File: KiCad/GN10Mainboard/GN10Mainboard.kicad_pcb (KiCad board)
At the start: 4 copper layers, 80 x 60 mm, 128 parts, among them J1 XT30PW-M, J10 USB_C_Receptacle_USB2.0, J12 Conn_01x04, J13 Conn_01x06, J14 Conn_01x06, J4 Conn_01x04, J5 Conn_01x06, J6 Conn_01x04, J7 Conn_01x04, J8 Conn_01x04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

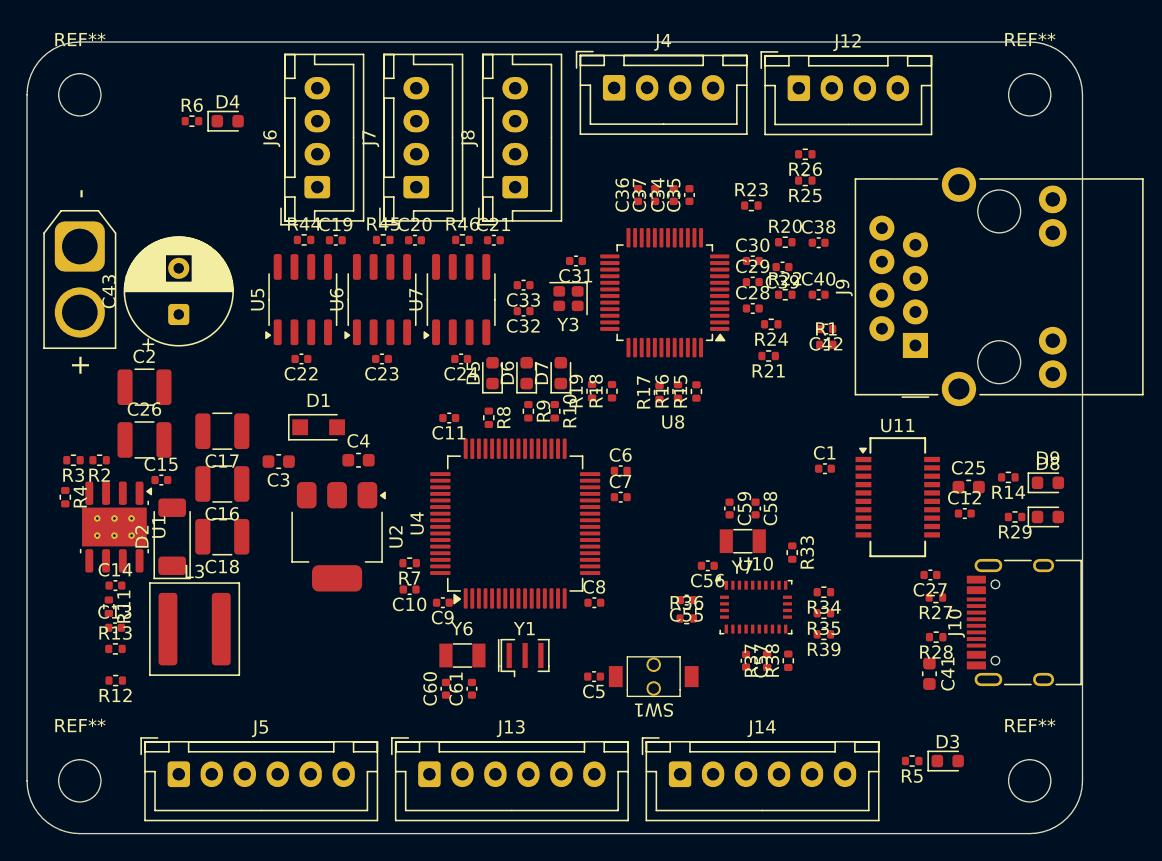
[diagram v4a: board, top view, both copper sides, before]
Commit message: update:compornents placement
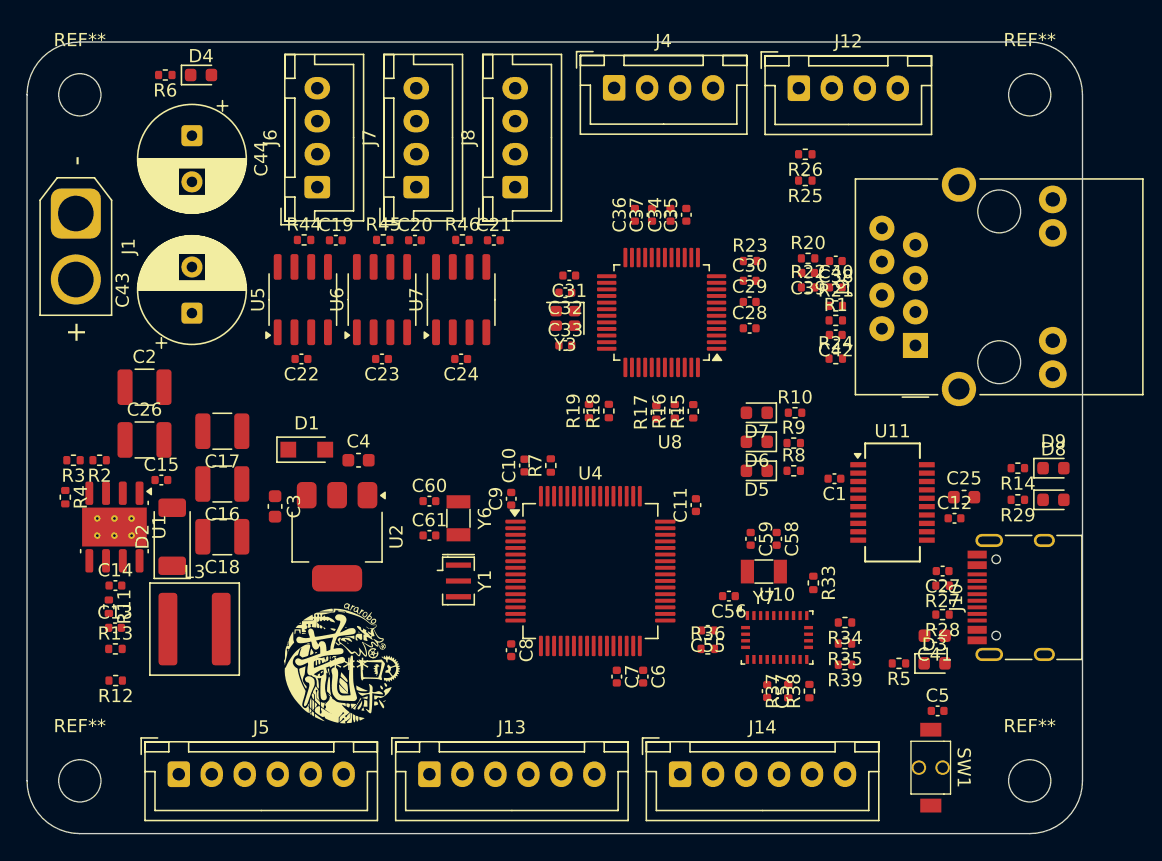
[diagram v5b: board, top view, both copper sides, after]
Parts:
- added C44: 100u, Capacitor_THT:CP_Radial_D8.0mm_P3.50mm, F.Cu at (142.5, 97.1)
- added G***: LOGO, GN10_Parts:ararobosmall, F.Cu at (153.6, 137.5)
- D2: value B560C -> RB088LAM-60TR
- moved C5 26.2 mm to (199.0, 140.7), turned to 0 degrees
- moved R8 23.5 mm to (188.1, 122.5), turned to 0 degrees
- moved SW1 22.1 mm to (198.5, 145.0), turned to -90 degrees
- moved D5 21.4 mm to (185.3, 122.5), turned to 180 degrees
- moved R9 20.3 mm to (188.1, 120.4), turned to 0 degrees
- moved C11 19.8 mm to (180.7, 125.1), turned to 90 degrees
- moved R10 18.2 mm to (188.2, 118.1), turned to 0 degrees
- moved D6 18.2 mm to (185.3, 120.3), turned to 180 degrees
- moved C6 15.7 mm to (176.7, 138.1), turned to -90 degrees
- moved D7 15.2 mm to (185.3, 118.1), turned to 180 degrees
- moved C60 14.3 mm to (160.5, 124.8), turned to 0 degrees
- moved C7 13.6 mm to (174.7, 138.1), turned to -90 degrees
- moved R7 13.0 mm to (169.7, 122.1), turned to 90 degrees
- moved C10 12.8 mm to (167.7, 122.1), turned to 90 degrees
- moved C61 12.1 mm to (160.5, 127.4), turned to 0 degrees
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
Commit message: update:components placement
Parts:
- moved R5 11.3 mm to (207.2, 139.3), turned to 0 degrees
- moved D3 6.12 mm to (204.5, 139.3), turned to 180 degrees
- moved C8 2.97 mm to (164.5, 134.1), turned to 180 degrees
- moved C17 2.81 mm to (145.0, 122.3)
- moved C16 2.11 mm to (145.0, 125.6)
- moved C43 1.66 mm to (140.8, 110.7), turned to 0 degrees
- moved C22 1.54 mm to (151.5, 115.4)
- moved C23 1.54 mm to (157.6, 115.4)
- moved C24 1.54 mm to (163.6, 115.4)
- moved C18 1.41 mm to (145.0, 128.9)
- moved U5 1.37 mm to (151.6, 110.7)
- moved U6 1.37 mm to (157.6, 110.7)
- moved U7 1.37 mm to (163.6, 110.7)
- moved C11 1.24 mm to (181.0, 126.3), turned to 0 degrees
- moved C10 1.21 mm to (168.8, 121.6)
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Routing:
- net +BATT: track 0.00 -> 8.51 mm

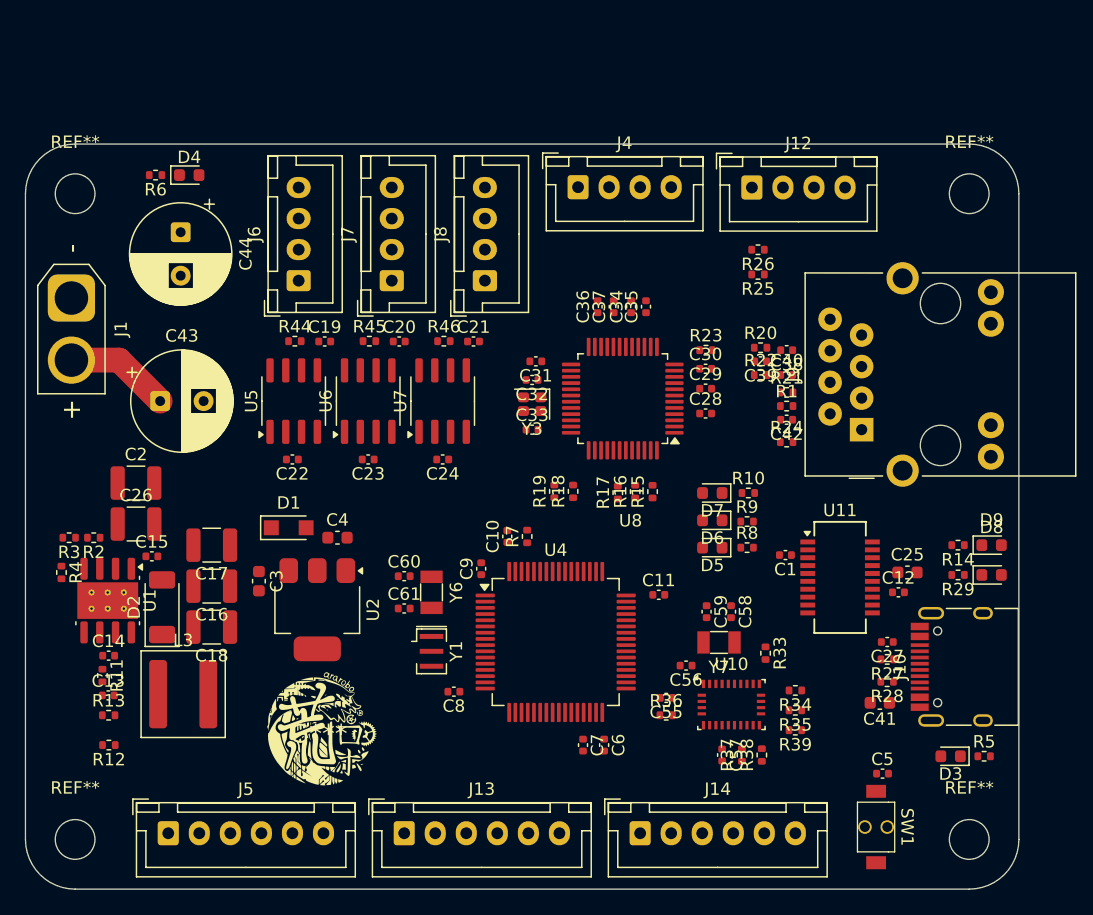
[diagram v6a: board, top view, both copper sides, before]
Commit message: add:DC/DC wiring
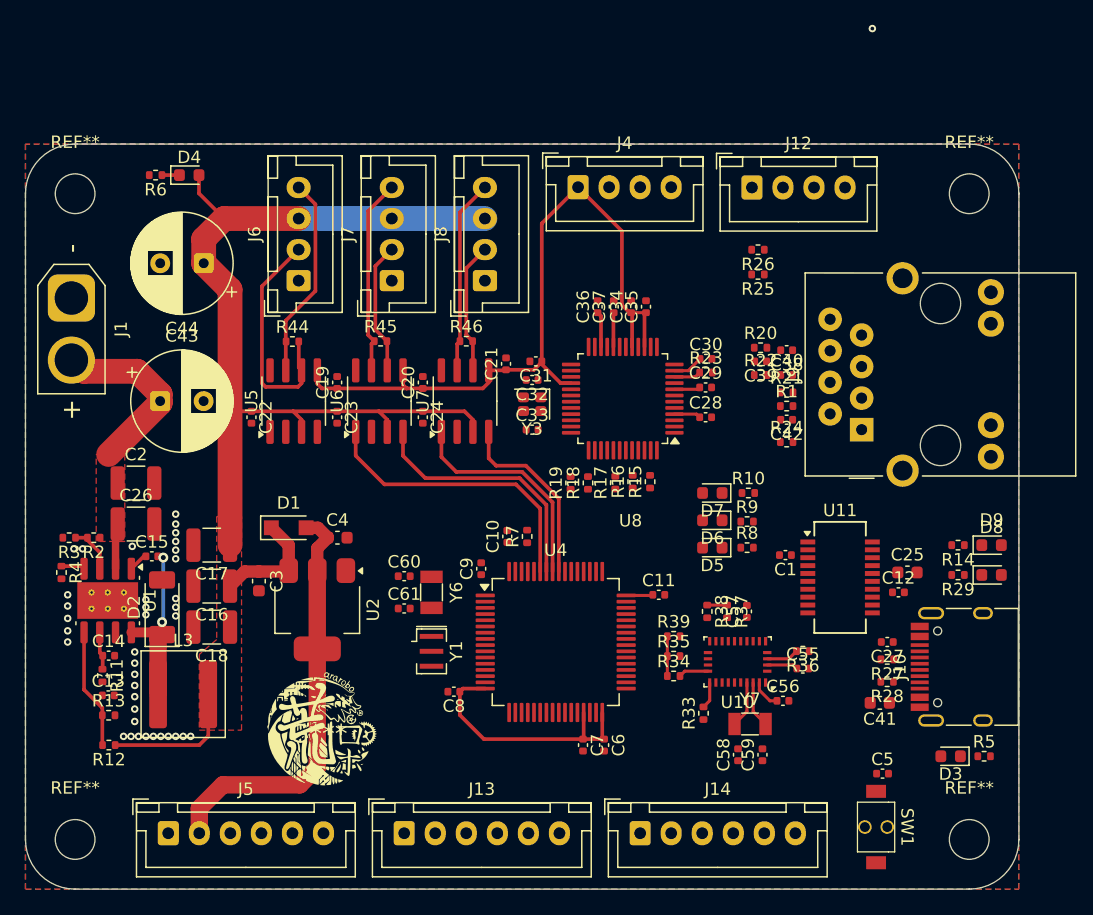
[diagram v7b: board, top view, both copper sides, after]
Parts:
- moved R39 12.4 mm to (182.2, 129.6), turned to 0 degrees
- moved R38 12.4 mm to (184.9, 127.6), turned to -90 degrees
- moved C59 12.4 mm to (189.3, 139.2), turned to 90 degrees
- moved R36 12.2 mm to (192.6, 130.8), turned to 180 degrees
- moved C57 11.7 mm to (188.1, 127.6), turned to 90 degrees
- moved R37 11.6 mm to (186.5, 127.6), turned to -90 degrees
- moved C58 11.5 mm to (187.4, 139.2), turned to 90 degrees
- moved C55 11.3 mm to (192.6, 132.2), turned to 0 degrees
- moved R35 10.7 mm to (182.2, 131.2), turned to 0 degrees
- moved R34 9.87 mm to (182.2, 132.8), turned to 0 degrees
- moved C56 8.30 mm to (191.0, 134.8), turned to 0 degrees
- moved Y7 7.02 mm to (188.3, 136.7), turned to 0 degrees
- moved R33 6.96 mm to (184.6, 135.8), turned to 90 degrees
- moved C22 4.73 mm to (148.2, 112.0), turned to -90 degrees
- moved C23 4.22 mm to (155.1, 112.0), turned to -90 degrees
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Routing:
- net +3.3V: track 0.00 -> 132.8 mm
- net +5V: track 0.00 -> 98.4 mm
- net CAN2_TX: track 0.00 -> 23.6 mm
- net CAN2_RX: track 0.00 -> 20.5 mm
- net CAN1_L: track 0.00 -> 18.9 mm
- net CAN3_TX: track 0.00 -> 18.1 mm
- net CAN1_H: track 0.00 -> 16.3 mm
- net CAN2_H: track 0.00 -> 15.8 mm
- net CAN3_H: track 0.00 -> 15.7 mm
- net CAN3_RX: track 0.00 -> 15.0 mm
- net Net-(D2-K): track 0.00 -> 14.2 mm, vias 0 -> 2
- net CAN2_L: track 0.00 -> 10.7 mm
- net CAN3_L: track 0.00 -> 10.6 mm
- net +BATT: track 8.51 -> 18.5 mm
- net Net-(U1-FB): track 0.00 -> 9.69 mm
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- added copper zone on F.Cu, net +5V
- added copper zone on F.Cu, net +BATT
- added copper zone on B.Cu, net GND
- added copper zone on F.Cu, net GND
- added copper zone on In1.Cu, net GND

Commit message: add:SPI wiring
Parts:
- moved R19 1.87 mm to (173.1, 115.6)
- moved C32 1.28 mm to (169.5, 109.1)
- moved C31 1.17 mm to (171.5, 108.6)
- moved R34 0.59 mm to (182.8, 132.9)
- moved R35 0.59 mm to (182.8, 131.3)
- moved R39 0.59 mm to (182.8, 129.7)
- moved Y1 0.55 mm to (162.7, 130.3)
- moved C33 0.45 mm to (170.6, 113.4), turned to 180 degrees
- moved C58 0.40 mm to (187.1, 138.9), turned to -90 degrees
- moved C59 0.38 mm to (189.6, 138.9), turned to -90 degrees
- moved Y3 0.32 mm to (170.6, 111.2), turned to -90 degrees
- moved R1 0.30 mm to (191.3, 111.4)
- moved C42 0.20 mm to (191.3, 112.4)
- moved C11 0.20 mm to (180.8, 126.3)
- moved R15 0.15 mm to (180.2, 117.3)
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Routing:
- net +3.3V: track 132.8 -> 237.3 mm
- net SPI1_SCK: track 0.00 -> 32.9 mm, vias 0 -> 2
- net SPI1_CS: track 0.00 -> 32.2 mm, vias 0 -> 2
- net SPI1_MISO: track 0.00 -> 29.6 mm, vias 0 -> 2
- net SPI1_MOSI: track 0.00 -> 26.4 mm, vias 0 -> 2
- net W5500_RST: track 0.00 -> 25.8 mm, vias 0 -> 2
- net Net-(J9-TD+): track 0.00 -> 18.8 mm
- net TIM3_CH2: track 0.00 -> 18.7 mm
- net TIM3_CH1: track 0.00 -> 17.1 mm
- net Net-(J9-TD-): track 0.00 -> 16.6 mm
- net Net-(U8-RXN): track 0.00 -> 12.2 mm, vias 0 -> 2
- net Net-(J9-RCT): track 0.00 -> 10.1 mm
- net Net-(U8-RXP): track 0.00 -> 9.94 mm, vias 0 -> 2
- net Net-(U11-CBUS1): track 0.00 -> 7.07 mm
- net Net-(U8-XI/CLKIN): track 0.00 -> 5.47 mm
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- added copper zone on F.Cu, net Net-(D2-K)
